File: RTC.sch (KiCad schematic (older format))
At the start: 5 parts, among them U12 PCF85063A, Y3 9HT12

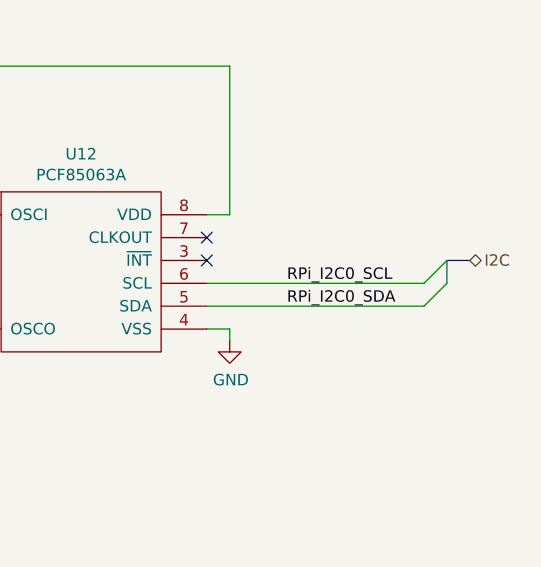
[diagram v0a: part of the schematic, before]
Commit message: - Bus Topologie entfernt - Levelshifter auf eigenes Blatt, abgeschlossen
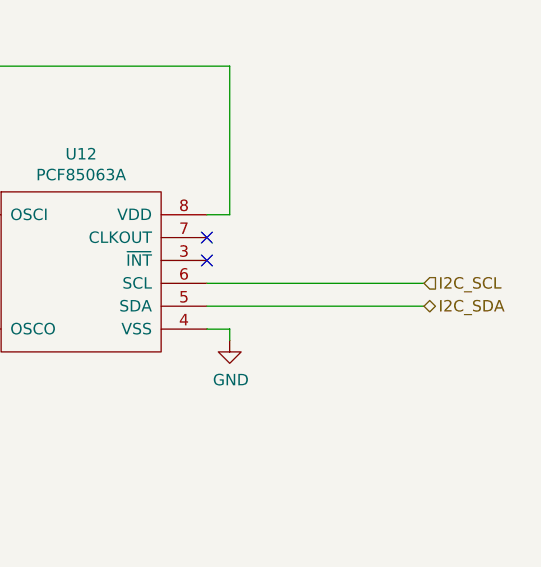
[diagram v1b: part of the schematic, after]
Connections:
- net RPi_I2C0_SCL renamed I2C_SCL
- net RPi_I2C0_SDA renamed I2C_SDA
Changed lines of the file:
@@
 $Descr A4 11693 8268
 encoding utf-8
-Sheet 7 8
+Sheet 4 9
 Title ""
 Date ""
@@
 	1    0    0    -1
 $EndComp
-Text Label 7000 4150 0    50   ~ 0
-RPi_I2C0_SCL
-Text Label 7000 4250 0    50   ~ 0
-RPi_I2C0_SDA
 $Comp
 L Device:Battery BT?
@@
 $EndComp
 NoConn ~ 6650 3950
-Wire Wire Line
-	6650 4150 7600 4150
-Wire Wire Line
-	6650 4250 7600 4250
 Wire Wire Line
 	6650 3850 6750 3850
@@
 Wire Wire Line
 	4700 4350 4700 3750
-Entry Wire Line
-	7600 4150 7700 4050
-Entry Wire Line
-	7600 4250 7700 4150
-Wire Bus Line
-	7700 4150 7700 4050
-Wire Bus Line
-	7700 4050 7800 4050
-Text HLabel 7800 4050 2    50   BiDi ~ 0
-I2C
+Text HLabel 7600 4250 2    50   BiDi ~ 0
+I2C_SDA
 Text Notes 4450 5800 0    50   ~ 0
 RTC nicht via doppelten hierarchischen Label\nRTC IC gewechselt jetzt mit Quarz\nBattery Holder so lieferbar?
+Wire Wire Line
+	6650 4250 7600 4250
+Wire Wire Line
+	6650 4150 7600 4150
+Text HLabel 7600 4150 2    50   Input ~ 0
+I2C_SCL
 $EndSCHEMATC

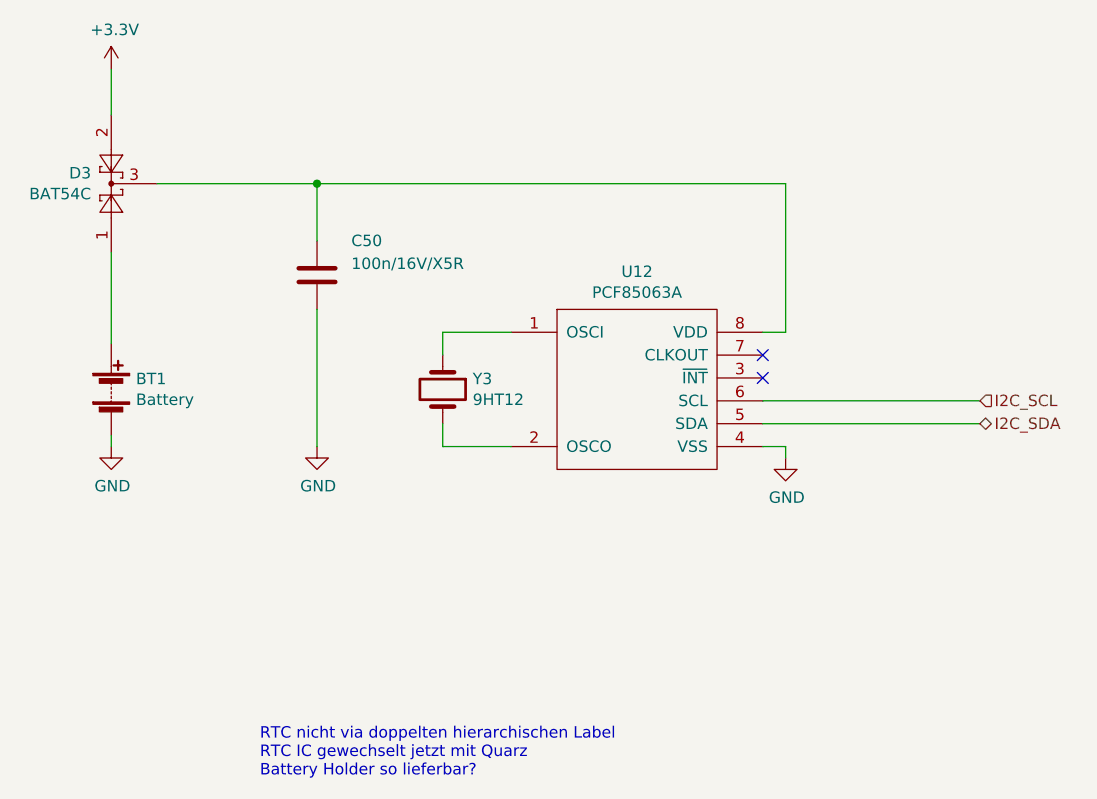
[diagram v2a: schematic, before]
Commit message: - ATmega überarbeitet - Alle offenen Punkte zusammengefasst
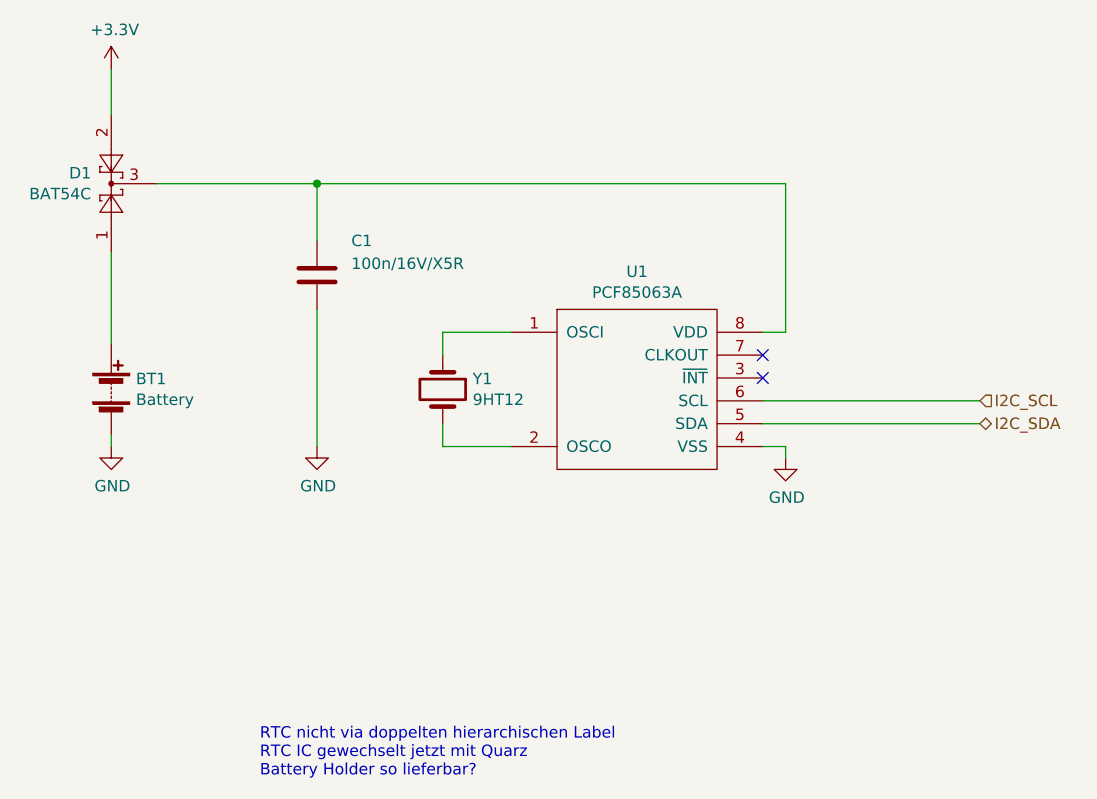
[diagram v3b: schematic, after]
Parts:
- renumbered C50 to C1, D3 to D1, U12 to U1, Y3 to Y1
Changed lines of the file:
@@
 $Descr A4 11693 8268
 encoding utf-8
-Sheet 3 9
+Sheet 2 9
 Title ""
 Date ""
@@
 P 4700 4350
 AR Path="/631EEDC8/649427DE" Ref="#PWR?"  Part="1"
-AR Path="/6493C3D2/649427DE" Ref="#PWR0125"  Part="1"
-F 0 "#PWR0125" H 4700 4100 50  0001 C CNN
+AR Path="/6493C3D2/649427DE" Ref="#PWR06"  Part="1"
+F 0 "#PWR06" H 4700 4100 50  0001 C CNN
 F 1 "GND" H 4705 4177 50  0000 C CNN
 F 2 "" H 4700 4350 50  0001 C CNN
@@
 AR Path="/614D7E9D/649427E4" Ref="C?"  Part="1"
 AR Path="/631EEDC8/649427E4" Ref="C?"  Part="1"
-AR Path="/6493C3D2/649427E4" Ref="C50"  Part="1"
-F 0 "C50" H 4850 3750 50  0000 L CNN
+AR Path="/6493C3D2/649427E4" Ref="C1"  Part="1"
+F 0 "C1" H 4850 3750 50  0000 L CNN
 F 1 "100n/16V/X5R" H 4850 3650 50  0000 L CNN
 F 2 "Capacitor_SMD:C_0603_1608Metric" H 4738 3450 50  0001 C CNN
@@
 P 3800 2700
 AR Path="/631EEDC8/649427EB" Ref="#PWR?"  Part="1"
-AR Path="/6493C3D2/649427EB" Ref="#PWR0123"  Part="1"
-F 0 "#PWR0123" H 3800 2550 50  0001 C CNN
+AR Path="/6493C3D2/649427EB" Ref="#PWR04"  Part="1"
+F 0 "#PWR04" H 3800 2550 50  0001 C CNN
 F 1 "+3.3V" H 3815 2873 50  0000 C CNN
 F 2 "" H 3800 2700 50  0001 C CNN
@@
 P 6100 4000
 AR Path="/631EEDC8/649427FE" Ref="U?"  Part="1"
-AR Path="/6493C3D2/649427FE" Ref="U12"  Part="1"
-F 0 "U12" H 6100 4415 50  0000 C CNN
+AR Path="/6493C3D2/649427FE" Ref="U1"  Part="1"
+F 0 "U1" H 6100 4415 50  0000 C CNN
 F 1 "PCF85063A" H 6100 4324 50  0000 C CNN
 F 2 "TeKaDe:SOT505-1" H 6100 3850 50  0001 C CNN
@@
 P 6750 4400
 AR Path="/631EEDC8/64942804" Ref="#PWR?"  Part="1"
-AR Path="/6493C3D2/64942804" Ref="#PWR0126"  Part="1"
-F 0 "#PWR0126" H 6750 4150 50  0001 C CNN
+AR Path="/6493C3D2/64942804" Ref="#PWR07"  Part="1"
+F 0 "#PWR07" H 6750 4150 50  0001 C CNN
 F 1 "GND" H 6755 4227 50  0000 C CNN
 F 2 "" H 6750 4400 50  0001 C CNN
@@
 P 3800 4350
 AR Path="/631EEDC8/64942810" Ref="#PWR?"  Part="1"
-AR Path="/6493C3D2/64942810" Ref="#PWR0124"  Part="1"
-F 0 "#PWR0124" H 3800 4100 50  0001 C CNN
+AR Path="/6493C3D2/64942810" Ref="#PWR05"  Part="1"
+F 0 "#PWR05" H 3800 4100 50  0001 C CNN
 F 1 "GND" H 3805 4177 50  0000 C CNN
 F 2 "" H 3800 4350 50  0001 C CNN
@@
 P 5250 4100
 AR Path="/631EEDC8/64942816" Ref="Y?"  Part="1"
-AR Path="/6493C3D2/64942816" Ref="Y3"  Part="1"
-F 0 "Y3" V 5204 4231 50  0000 L CNN
+AR Path="/6493C3D2/64942816" Ref="Y1"  Part="1"
+F 0 "Y1" V 5204 4231 50  0000 L CNN
 F 1 "9HT12" V 5295 4231 50  0000 L CNN
 F 2 "Crystal:Crystal_SMD_MicroCrystal_CM9V-T1A-2Pin_1.6x1.0mm" H 5250 4100 50  0001 C CNN
@@
 P 3800 3200
 AR Path="/631EEDC8/64942822" Ref="D?"  Part="1"
-AR Path="/6493C3D2/64942822" Ref="D3"  Part="1"
-F 0 "D3" V 3846 3288 50  0000 L CNN
+AR Path="/6493C3D2/64942822" Ref="D1"  Part="1"
+F 0 "D1" V 3846 3288 50  0000 L CNN
 F 1 "BAT54C" V 3755 3288 50  0000 L CNN
 F 2 "Package_TO_SOT_SMD:SOT-23" H 3875 3325 50  0001 L CNN

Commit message: - Platzoptimierungen
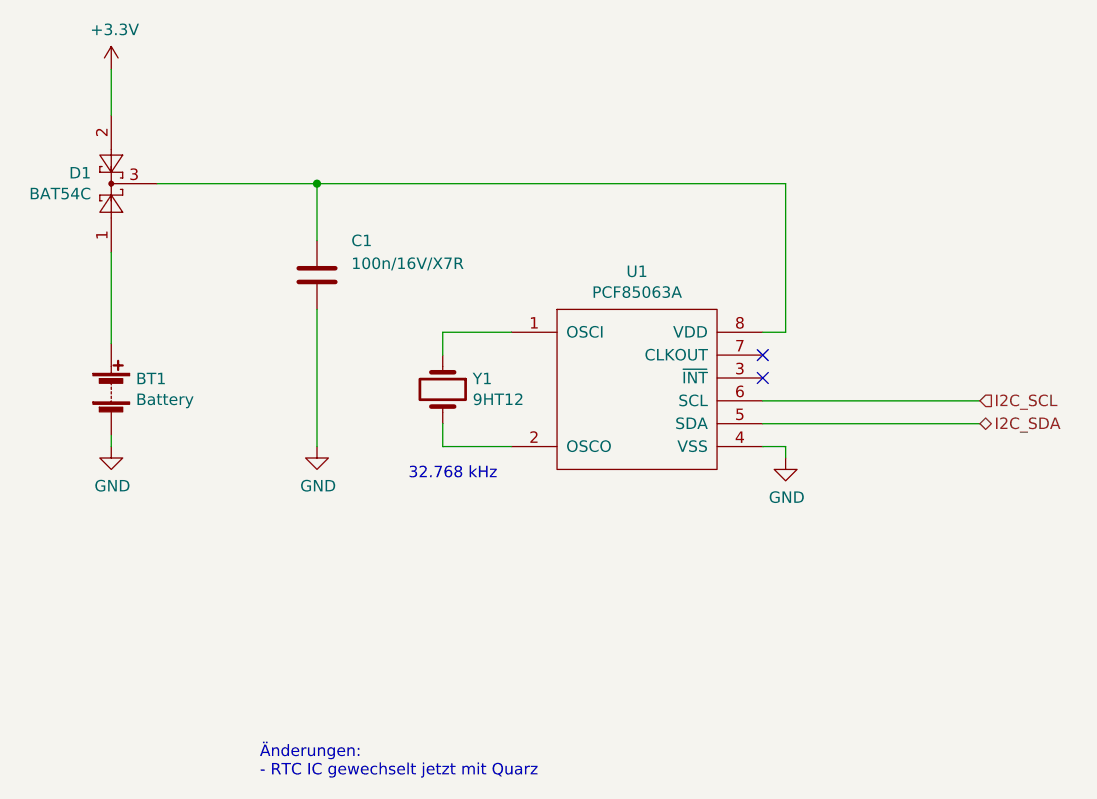
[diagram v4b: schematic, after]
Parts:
- C1: value 100n/16V/X5R -> 100n/16V/X7R; footprint Capacitor_SMD:C_0603_1608Metric -> Capacitor_SMD:C_0402_1005Metric
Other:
- note added: "32.768 kHz"
- note added: "Änderungen:\n- RTC IC gewechselt jetzt mit Quarz"
- note removed: "RTC nicht via doppelten hierarchischen Label\nRTC IC gewechselt jetzt mit Quarz\nBattery Holder so lieferbar?"
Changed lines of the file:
@@
 AR Path="/6493C3D2/649427E4" Ref="C1"  Part="1"
 F 0 "C1" H 4850 3750 50  0000 L CNN
-F 1 "100n/16V/X5R" H 4850 3650 50  0000 L CNN
-F 2 "Capacitor_SMD:C_0603_1608Metric" H 4738 3450 50  0001 C CNN
+F 1 "100n/16V/X7R" H 4850 3650 50  0000 L CNN
+F 2 "Capacitor_SMD:C_0402_1005Metric" H 4738 3450 50  0001 C CNN
 F 3 "~" H 4700 3600 50  0001 C CNN
 	1    4700 3600
@@
 I2C_SDA
 Text Notes 4450 5800 0    50   ~ 0
-RTC nicht via doppelten hierarchischen Label\nRTC IC gewechselt jetzt mit Quarz\nBattery Holder so lieferbar?
+Änderungen:\n- RTC IC gewechselt jetzt mit Quarz
 Wire Wire Line
 	6650 4250 7600 4250
@@
 Text HLabel 7600 4150 2    50   Input ~ 0
 I2C_SCL
+Text Notes 5100 4500 0    50   ~ 0
+32.768 kHz
 $EndSCHEMATC

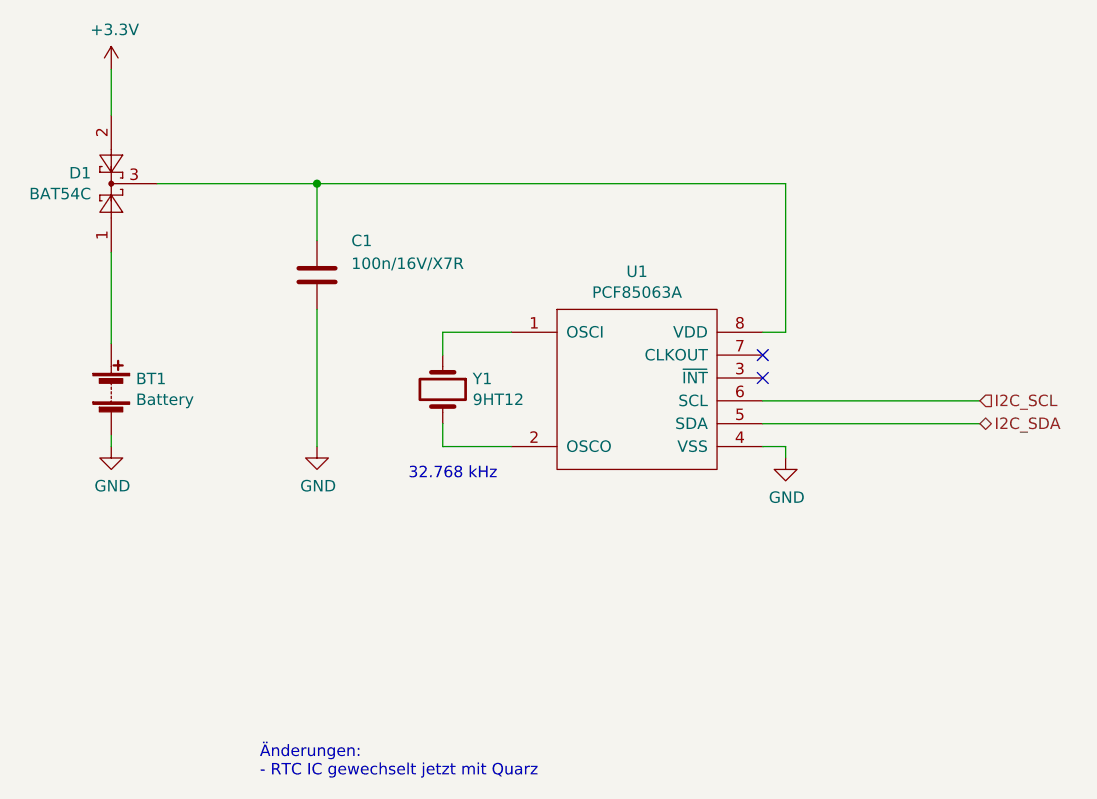
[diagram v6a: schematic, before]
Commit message: - Schaltbare BL Versorgung fertig - kleinere Value Anpassungen - Finale Annotation
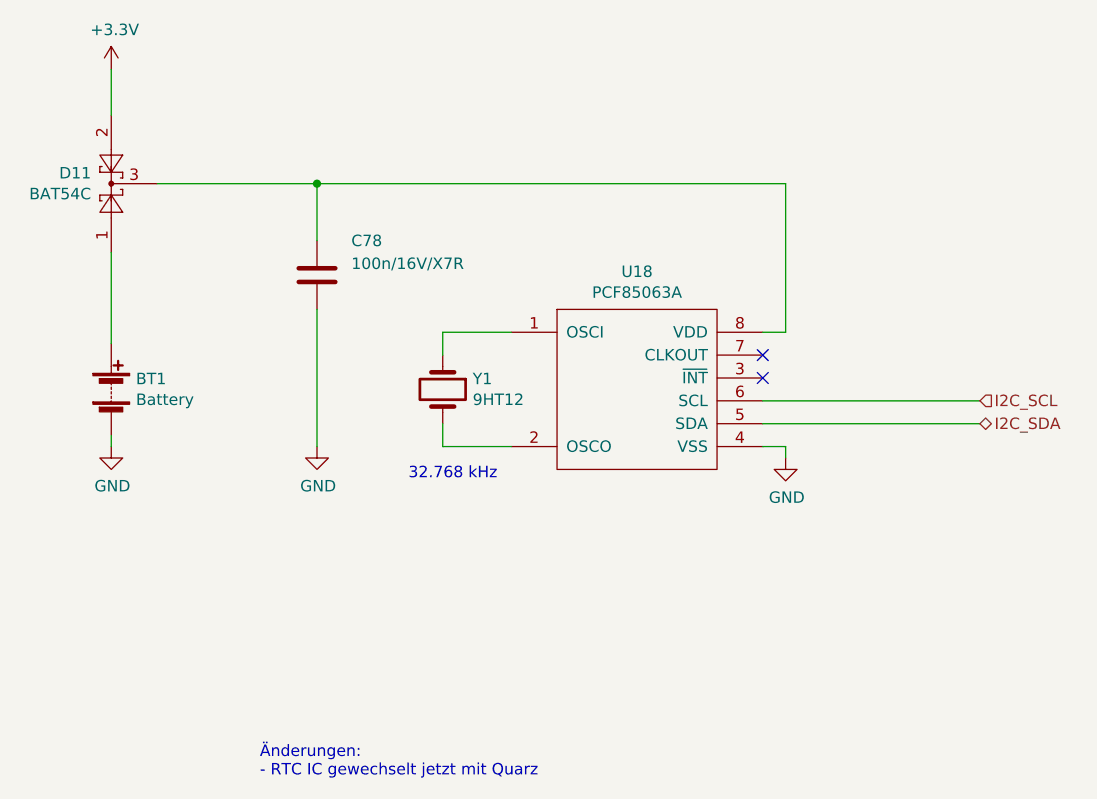
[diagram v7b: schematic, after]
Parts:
- renumbered C1 to C78, D1 to D11, U1 to U18
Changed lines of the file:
@@
 $Descr A4 11693 8268
 encoding utf-8
-Sheet 2 9
+Sheet 9 9
 Title ""
 Date ""
@@
 P 4700 4350
 AR Path="/631EEDC8/649427DE" Ref="#PWR?"  Part="1"
-AR Path="/6493C3D2/649427DE" Ref="#PWR06"  Part="1"
-F 0 "#PWR06" H 4700 4100 50  0001 C CNN
+AR Path="/6493C3D2/649427DE" Ref="#PWR0181"  Part="1"
+F 0 "#PWR0181" H 4700 4100 50  0001 C CNN
 F 1 "GND" H 4705 4177 50  0000 C CNN
 F 2 "" H 4700 4350 50  0001 C CNN
@@
 AR Path="/614D7E9D/649427E4" Ref="C?"  Part="1"
 AR Path="/631EEDC8/649427E4" Ref="C?"  Part="1"
-AR Path="/6493C3D2/649427E4" Ref="C1"  Part="1"
-F 0 "C1" H 4850 3750 50  0000 L CNN
+AR Path="/6493C3D2/649427E4" Ref="C78"  Part="1"
+F 0 "C78" H 4850 3750 50  0000 L CNN
 F 1 "100n/16V/X7R" H 4850 3650 50  0000 L CNN
 F 2 "Capacitor_SMD:C_0402_1005Metric" H 4738 3450 50  0001 C CNN
@@
 P 3800 2700
 AR Path="/631EEDC8/649427EB" Ref="#PWR?"  Part="1"
-AR Path="/6493C3D2/649427EB" Ref="#PWR04"  Part="1"
-F 0 "#PWR04" H 3800 2550 50  0001 C CNN
+AR Path="/6493C3D2/649427EB" Ref="#PWR0179"  Part="1"
+F 0 "#PWR0179" H 3800 2550 50  0001 C CNN
 F 1 "+3.3V" H 3815 2873 50  0000 C CNN
 F 2 "" H 3800 2700 50  0001 C CNN
@@
 P 6100 4000
 AR Path="/631EEDC8/649427FE" Ref="U?"  Part="1"
-AR Path="/6493C3D2/649427FE" Ref="U1"  Part="1"
-F 0 "U1" H 6100 4415 50  0000 C CNN
+AR Path="/6493C3D2/649427FE" Ref="U18"  Part="1"
+F 0 "U18" H 6100 4415 50  0000 C CNN
 F 1 "PCF85063A" H 6100 4324 50  0000 C CNN
 F 2 "TeKaDe:SOT505-1" H 6100 3850 50  0001 C CNN
@@
 P 6750 4400
 AR Path="/631EEDC8/64942804" Ref="#PWR?"  Part="1"
-AR Path="/6493C3D2/64942804" Ref="#PWR07"  Part="1"
-F 0 "#PWR07" H 6750 4150 50  0001 C CNN
+AR Path="/6493C3D2/64942804" Ref="#PWR0182"  Part="1"
+F 0 "#PWR0182" H 6750 4150 50  0001 C CNN
 F 1 "GND" H 6755 4227 50  0000 C CNN
 F 2 "" H 6750 4400 50  0001 C CNN
@@
 P 3800 4350
 AR Path="/631EEDC8/64942810" Ref="#PWR?"  Part="1"
-AR Path="/6493C3D2/64942810" Ref="#PWR05"  Part="1"
-F 0 "#PWR05" H 3800 4100 50  0001 C CNN
+AR Path="/6493C3D2/64942810" Ref="#PWR0180"  Part="1"
+F 0 "#PWR0180" H 3800 4100 50  0001 C CNN
 F 1 "GND" H 3805 4177 50  0000 C CNN
 F 2 "" H 3800 4350 50  0001 C CNN
@@
 P 3800 3200
 AR Path="/631EEDC8/64942822" Ref="D?"  Part="1"
-AR Path="/6493C3D2/64942822" Ref="D1"  Part="1"
-F 0 "D1" V 3846 3288 50  0000 L CNN
+AR Path="/6493C3D2/64942822" Ref="D11"  Part="1"
+F 0 "D11" V 3846 3288 50  0000 L CNN
 F 1 "BAT54C" V 3755 3288 50  0000 L CNN
 F 2 "Package_TO_SOT_SMD:SOT-23" H 3875 3325 50  0001 L CNN

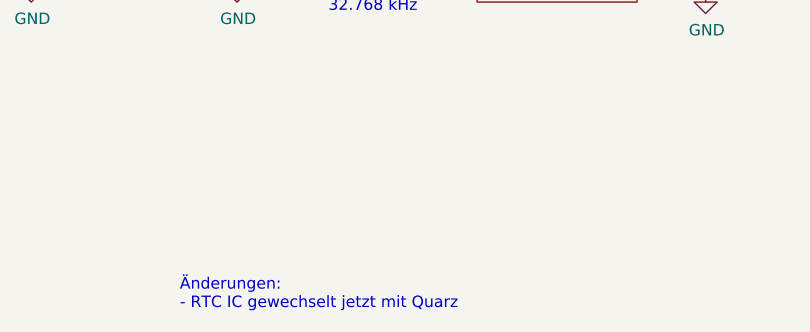
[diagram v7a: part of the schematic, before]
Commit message: - Layout Zwischenstand, UI Board Ansteuerung fast fertig - GPIOs von ATmega komplett umsortiert - Darlington Anschlüsse umsortiert
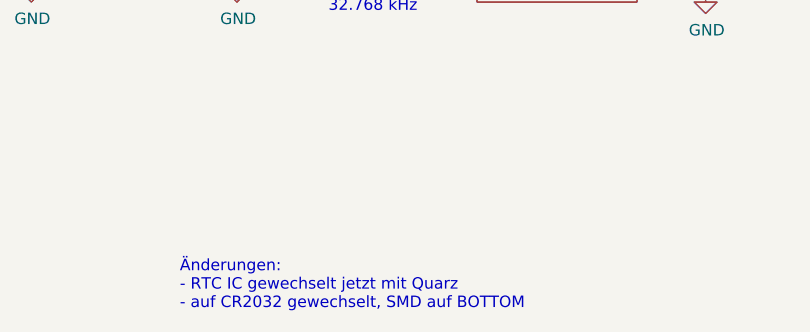
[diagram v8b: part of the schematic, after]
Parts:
- BT1: footprint TeKaDeConn:CR1220 -> Battery:BatteryHolder_MPD_BC2003_1x2032
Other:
- note added: "Änderungen:\n- RTC IC gewechselt jetzt mit Quarz\n- auf CR2032 gewechselt, SMD auf BOTTOM"
- note removed: "Änderungen:\n- RTC IC gewechselt jetzt mit Quarz"
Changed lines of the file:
@@
 F 0 "BT1" H 3908 4146 50  0000 L CNN
 F 1 "Battery" H 3908 4055 50  0000 L CNN
-F 2 "TeKaDeConn:CR1220" V 3800 4160 50  0001 C CNN
+F 2 "Battery:BatteryHolder_MPD_BC2003_1x2032" V 3800 4160 50  0001 C CNN
 F 3 "~" V 3800 4160 50  0001 C CNN
 	1    3800 4100
@@
 I2C_SDA
 Text Notes 4450 5800 0    50   ~ 0
-Änderungen:\n- RTC IC gewechselt jetzt mit Quarz
+Änderungen:\n- RTC IC gewechselt jetzt mit Quarz\n- auf CR2032 gewechselt, SMD auf BOTTOM
 Wire Wire Line
 	6650 4250 7600 4250
